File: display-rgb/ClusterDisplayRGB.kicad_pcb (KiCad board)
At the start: 4 copper layers, 211 x 101.8 mm, 137 parts, among them J1 Verdin iMX95 Hexa 8GB WB IT, J10 RTC coin cell, J11 Molex KK-254 22-27-2041, rota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, J12 Samtec TSW-103-07-G-S A55 con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, J13 Samtec TSW-105-07-G-S USB_1 O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, J14 PLACEHOLDER 50-pin FPC for th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, J2 Phoenix MKDS 1,5/3-5,08 power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, J3 Molex KK-254 22-27-2031 priva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, J4 TST040HDBC-42 panel, J8 Samtec TSW-108-07-G-S JTAG (b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, J9 Samtec TSW-104-07-G-S buttons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, Q1 PMV55ENEA (AEC-Q101, 60V/20V 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, Q2 PMV55ENEA (AEC-Q101, 60V/20V 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, Q3 PMV55ENEA ignition wake pulld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, U1 LM74930-Q1, U10 TLV733P-Q1 3.3V (AEC-Q100 G1), U2 LM61460-Q1, U3 TLV767-Q1, U4 TCAN1044V-Q1, U6 TPS65131-Q1, U7 TPS61165-Q1, U8 TPS22918-Q1 (AEC-Q100 G2) dia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, U9 DS90CF384AQ-Q1

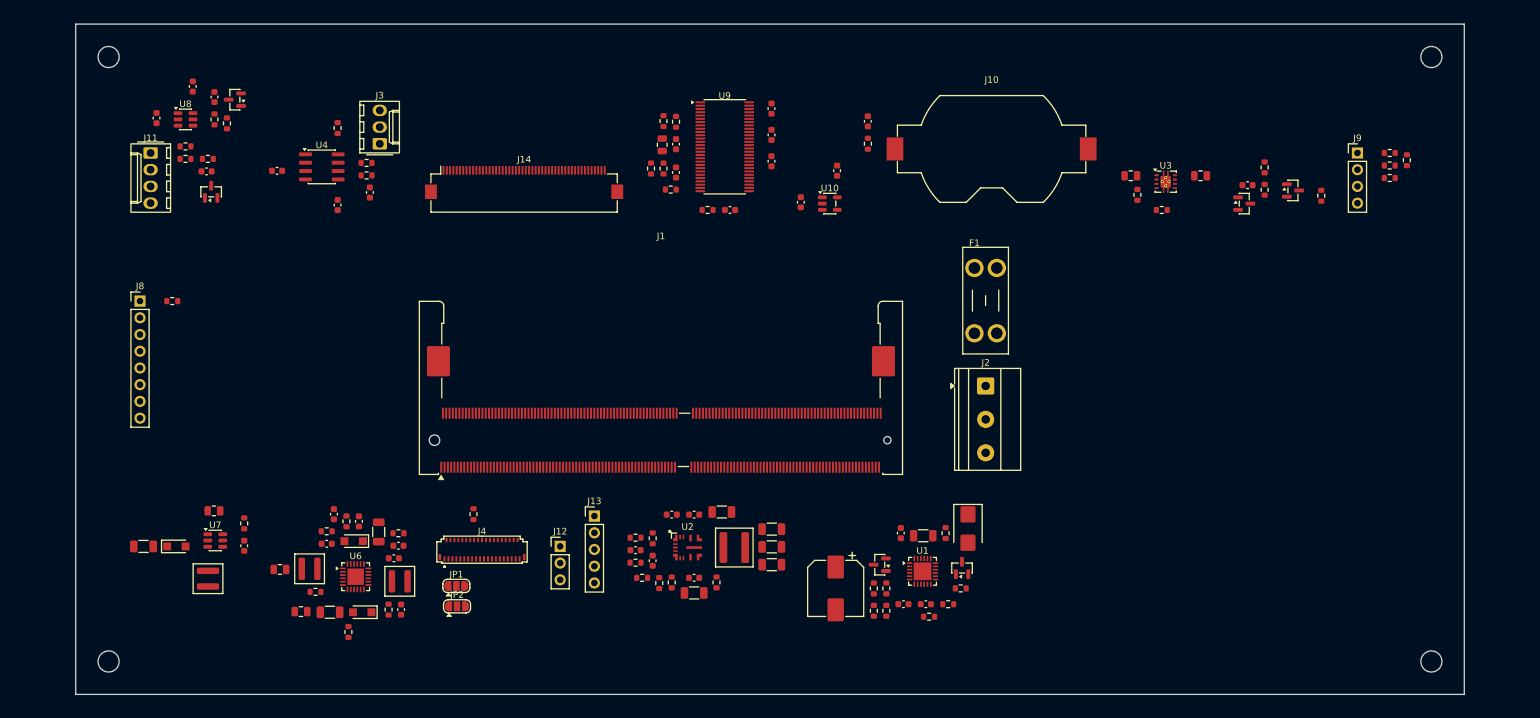
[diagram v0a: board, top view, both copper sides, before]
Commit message: Six layers with solid GND planes, a field-solved DSI geometry, and the RGB variant routed
Both boards and display-rgb/ move to JLC06161H-3313 six-layer: F / In1 GND /
In2 / In3 with the +5V or +3V3 pour / In4 GND / B. Every net class except GND
is restricted to F, In2, In3 and B in the router input (FreeRouting 2.2.4
ignores a layer_rule "active off"), and review/layout_checks.py now fails a
board with any track on In1 or In4. All three boards: 0 unconnected under
kicad-cli DRC, accepted categories only, no copper but GND fill on the planes.

- DSI pairs are 0.16 mm, field-solved on the new stack-up at 96.4-103.1 ohm
  differential (review/dsi_impedance.py); board minimum track 0.15 mm.
- gauges/ routes VIN_PROT, VIN_FUSED and +5V at 0.4 mm from the start; every
  power net now passes the 20 K current check, and nothing crosses the buck's
  switch node (P-07).
- Panel bias +5.98 V / -6.05 V, inside the ICNL9707's rating; fab/README.md
  gives a diode-test check of the panel's pin polarity before JP1/JP2.
- display-rgb/ brought up to date with display/ (standoffs, FETs, audio,
  USB-C, MFi header), RGB parts renumbered, routed; still not a fab candidate
  while its panel connector is a placeholder.
- FreeRouting runs end at routing: (postroute off) in the DSN, a job timeout
  as backstop; one in-place attempt, since retries of one DSN are identical.
- The OV/UV divider tops are pulled to the LM74930 SW pin.
- docs/electrical-review.md section 8b records the measured results; the
  display/ battery path on inner copper (D-02 residual) is still open.

Co-Authored-By: Claude Opus 5.5 <noreply@anthropic.com>
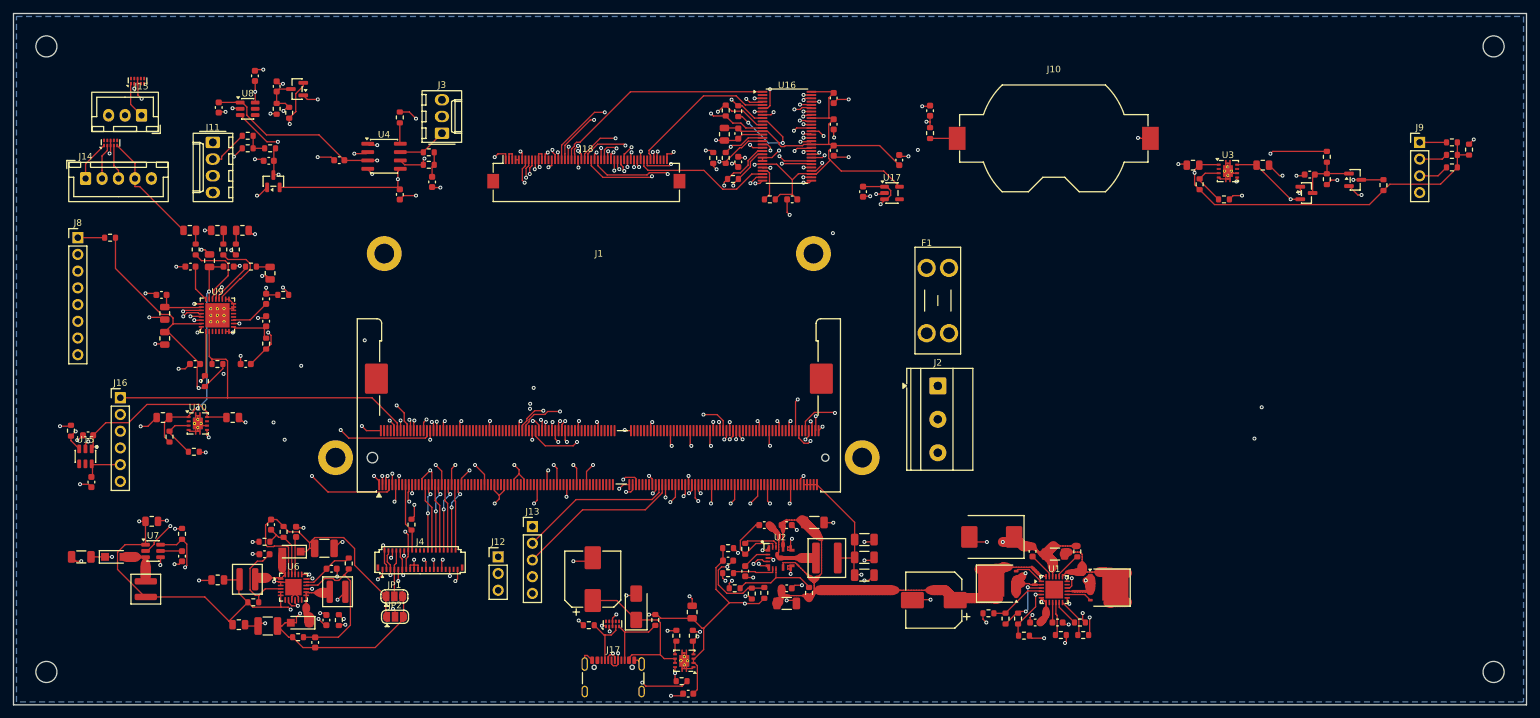
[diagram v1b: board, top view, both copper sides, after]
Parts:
- added C73: 1u MICBIAS, Capacitor_SMD:C_0603_1608Metric, F.Cu at (133.5, 142.7)
- added C74: 1u mic AC couple, Capacitor_SMD:C_0603_1608Metric, F.Cu at (130.4, 149.2)
- added C75: 1u mic AC couple, Capacitor_SMD:C_0603_1608Metric, F.Cu at (133.5, 139.3)
- added C76: 4.7u line-out DC block, Capacitor_SMD:C_0805_2012Metric, F.Cu at (134.1, 135.4)
- added C77: 4.7u line-out DC block, Capacitor_SMD:C_0805_2012Metric, F.Cu at (126.1, 128.9)
- added C78: 4.7u line-out DC block, Capacitor_SMD:C_0805_2012Metric, F.Cu at (129.9, 128.9)
- added C79: 4.7u line-out DC block, Capacitor_SMD:C_0805_2012Metric, F.Cu at (121.9, 128.9)
- added C80: 100n USB switch IN, Capacitor_SMD:C_0603_1608Metric, F.Cu at (197.6, 199.3)
- added C81: 10u USB switch IN, Capacitor_SMD:C_0805_2012Metric, F.Cu at (198.2, 186.9)
- added C82: 100u 35V hybrid polymer VBUS (Panasonic EEH-ZA1V101P), Capacitor_SMD:CP_Elec_8x10, F.Cu at (183.1, 181.9)
- added C83: 1u MFi switch CIN, Capacitor_SMD:C_0603_1608Metric, F.Cu at (106.4, 160.1)
- added C84: 1u MFi 5V out, Capacitor_SMD:C_0603_1608Metric, F.Cu at (106.9, 167.2)
- added C85: 1u LDO input (AEC-Q200), Capacitor_SMD:C_0603_1608Metric, F.Cu at (224.1, 123.0)
- added C86: 1u LDO output (AEC-Q200), Capacitor_SMD:C_0603_1608Metric, F.Cu at (229.6, 118.2)
- added C87: 100n receiver VCC decoupling (AEC-Q200), Capacitor_SMD:C_0603_1608Metric, F.Cu at (213.4, 124.2)
- added C88: 100n receiver VCC decoupling (AEC-Q200), Capacitor_SMD:C_0603_1608Metric, F.Cu at (219.7, 116.8)
- added C89: 100n receiver VCC decoupling (AEC-Q200), Capacitor_SMD:C_0603_1608Metric, F.Cu at (219.7, 112.8)
- added C90: 100n receiver VCC decoupling (AEC-Q200), Capacitor_SMD:C_0603_1608Metric, F.Cu at (219.7, 108.8)
- added C91: 100n receiver VCC decoupling (AEC-Q200), Capacitor_SMD:C_0603_1608Metric, F.Cu at (205.2, 114.2)
- added C92: 100n receiver VCC decoupling (AEC-Q200), Capacitor_SMD:C_0603_1608Metric, F.Cu at (205.2, 118.5)
- added C93: 10u receiver bulk (AEC-Q200), Capacitor_SMD:C_0805_2012Metric, F.Cu at (203.1, 114.3)
- added D8: SMAJ5.0A VBUS TVS, Diode_SMD:D_SMA, F.Cu at (189.7, 186.1)
- added J15: JST XH B3B-XH-A electret microphone (2-wire + shield), Connector_JST:JST_XH_B3B-XH-A_1x03_P2.50mm_Vertical, F.Cu at (114.5, 111.5)
- added J16: MFi daughterboard header I2C_1, reset, switched 5V, 1V8 (DN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, Connector_PinHeader_2.54mm:PinHeader_1x06_P2.54mm_Vertical, F.Cu at (111.3, 154.4)
- added J17: GCT USB4105-GF-A USB-C 2.0 host receptacle, Connector_USB:USB_C_Receptacle_GCT_USB4105-xx-A_16P_TopMnt_Horizontal, F.Cu at (186.2, 197.9)
- added J18: PLACEHOLDER 50-pin FPC for the RGB panel (pinout TBD), Connector_FFC-FPC:Hirose_FH12-50S-0.5SH_1x50-1MP_P0.50mm_Horizontal, F.Cu at (182.1, 120.0)
- added R65: 100R line-out series, Resistor_SMD:R_0603_1608Metric, F.Cu at (131.2, 134.4)
- added R66: 100R line-out series, Resistor_SMD:R_0603_1608Metric, F.Cu at (127.0, 131.8)
- added R67: 100R line-out series, Resistor_SMD:R_0603_1608Metric, F.Cu at (128.9, 131.8)
- added R68: 100R line-out series, Resistor_SMD:R_0603_1608Metric, F.Cu at (122.8, 131.8)
- added R69: 61.9k 1% USB ILIM (1.6-2.0 A), Resistor_SMD:R_0603_1608Metric, F.Cu at (195.8, 190.5)
- added R70: 100k FAULT pull-up to +1V8, Resistor_SMD:R_0603_1608Metric, F.Cu at (196.6, 197.4)
- added R71: 22k Rp CC1 (1.5 A, +/-5 percent or better), Resistor_SMD:R_0603_1608Metric, F.Cu at (182.5, 188.9)
- added R72: 22k Rp CC2 (1.5 A, +/-5 percent or better), Resistor_SMD:R_0603_1608Metric, F.Cu at (192.6, 188.1)
- added R73: 100k USB EN pull-down, Resistor_SMD:R_0603_1608Metric, F.Cu at (198.3, 190.5)
- added R74: 100k MFi switch off in reset, Resistor_SMD:R_0603_1608Metric, F.Cu at (103.8, 159.4)
- added R75: 100R LVDS pair termination, Resistor_SMD:R_0603_1608Metric, F.Cu at (205.2, 110.8)
- added R76: 100R LVDS pair termination, Resistor_SMD:R_0603_1608Metric, F.Cu at (203.3, 110.7)
- added R77: 100R LVDS pair termination, Resistor_SMD:R_0603_1608Metric, F.Cu at (203.3, 117.9)
- added R78: 100R LVDS pair termination, Resistor_SMD:R_0603_1608Metric, F.Cu at (204.4, 121.1)
- added R79: 100R LVDS pair termination, Resistor_SMD:R_0603_1608Metric, F.Cu at (201.4, 117.9)
- added R80: 10k PWR_DWN pull-up (always enabled), Resistor_SMD:R_0603_1608Metric, F.Cu at (210.0, 124.2)
- added S1: M2x0.4 SMD standoff 2.5 mm, MountingHole:MountingHole_2.2mm_M2_Pad, F.Cu at (151.4, 132.5)
- added S2: M2x0.4 SMD standoff 2.5 mm, MountingHole:MountingHole_2.2mm_M2_Pad, F.Cu at (216.6, 132.5)
- added S3: M2x0.4 SMD standoff 7.0 mm, MountingHole:MountingHole_2.2mm_M2_Pad, F.Cu at (144.0, 163.5)
- added S4: M2x0.4 SMD standoff 7.0 mm, MountingHole:MountingHole_2.2mm_M2_Pad, F.Cu at (224.0, 163.5)
- added U11: TPS2557-Q1, Package_DFN_QFN:Texas_DRB0008A, F.Cu at (197.0, 194.3)
- added U12: TPD4E02B04-Q1 line-out ESD (bidirectional, review D-11), Package_SON:USON-10_2.5x1.0mm_P0.5mm, F.Cu at (109.8, 115.7)
- added U13: TPD4E05U06-Q1 mic ESD, Package_SON:USON-10_2.5x1.0mm_P0.5mm, F.Cu at (113.9, 106.2)
- added U14: TPD4E05U06-Q1 USB ESD, Package_SON:USON-10_2.5x1.0mm_P0.5mm, F.Cu at (186.1, 188.7)
- added U15: TPS22918-Q1 (AEC-Q100 G2) MFi 5V switch, Package_TO_SOT_SMD:SOT-23-6, F.Cu at (106.0, 163.3)
- added U16: DS90CF384AQ-Q1, Package_SO:TSSOP-56_6.1x14mm_P0.5mm, F.Cu at (212.6, 114.6)
- added U17: TLV733P-Q1 3.3V (AEC-Q100 G1), Package_TO_SOT_SMD:SOT-23-5, F.Cu at (228.5, 123.2)
- C46, C47: footprint Capacitor_SMD:C_1206_3216Metric -> Capacitor_SMD:C_1210_3225Metric
- C64: value 1u LDO input (AEC-Q200) -> 10u CIN; footprint Capacitor_SMD:C_0603_1608Metric -> Capacitor_SMD:C_0805_2012Metric
- C65: value 1u LDO output (AEC-Q200) -> 10u COUT; footprint Capacitor_SMD:C_0603_1608Metric -> Capacitor_SMD:C_0805_2012Metric
- C66: value 100n receiver VCC decoupling (AEC-Q200) -> 10u AVDD; footprint Capacitor_SMD:C_0603_1608Metric -> Capacitor_SMD:C_0805_2012Metric
- C67: value 100n receiver VCC decoupling (AEC-Q200) -> 100n AVDD
- C68: value 100n receiver VCC decoupling (AEC-Q200) -> 10u DREG; footprint Capacitor_SMD:C_0603_1608Metric -> Capacitor_SMD:C_0805_2012Metric
- C69: value 100n receiver VCC decoupling (AEC-Q200) -> 100n DREG
- C70: value 100n receiver VCC decoupling (AEC-Q200) -> 10u IOVDD; footprint Capacitor_SMD:C_0603_1608Metric -> Capacitor_SMD:C_0805_2012Metric
- C71: value 100n receiver VCC decoupling (AEC-Q200) -> 100n IOVDD
- C72: value 10u receiver bulk (AEC-Q200) -> 1u VREF; footprint Capacitor_SMD:C_0805_2012Metric -> Capacitor_SMD:C_0603_1608Metric
- D1: footprint Diode_SMD:D_SMB -> Diode_SMD:D_SMC
- J14: value PLACEHOLDER 50-pin FPC for the RGB panel (pinout TBD) -> JST XH B5B-XH-A balanced line-out L/R; footprint Connector_FFC-FPC:Hirose_FH12-50S-0.5SH_1x50-1MP_P0.50mm_Horizontal -> Connector_JST:JST_XH_B5B-XH-A_1x05_P2.50mm_Vertical
- Q1: value PMV55ENEA (AEC-Q101, 60V/20V VGS) diode -> SQJ460AEP (AEC-Q101, 60V/20V VGS) diode; footprint Package_TO_SOT_SMD:SOT-23 -> Package_SO:PowerPAK_SO-8L_Single
- Q2: value PMV55ENEA (AEC-Q101, 60V/20V VGS) pass -> SQJ460AEP (AEC-Q101, 60V/20V VGS) pass; footprint Package_TO_SOT_SMD:SOT-23 -> Package_SO:PowerPAK_SO-8L_Single
- R38: value 562k VPOS top R1 (see docstring) -> 511k VPOS top R1 (see docstring)
- R40: value 536k VNEG top R3 (see docstring) -> 499k VNEG top R3 (see docstring)
- R59: value 100R LVDS pair termination -> 316k 1% FB top
- R60: value 100R LVDS pair termination -> 100k FB bot
- R61: value 100R LVDS pair termination -> 2.2k I2C1 SDA pull-up
- R62: value 100R LVDS pair termination -> 2.2k I2C1 SCL pull-up
- R63: value 100R LVDS pair termination -> 2.2k mic bias
- R64: value 10k PWR_DWN pull-up (always enabled) -> 100R mic return
- U10: value TLV733P-Q1 3.3V (AEC-Q100 G1) -> TLV767-Q1 (3.3 V audio AVDD); footprint Package_TO_SOT_SMD:SOT-23-5 -> Package_DFN_QFN:Texas_DRB0008A
- U9: value DS90CF384AQ-Q1 -> TAC5112-Q1; footprint Package_SO:TSSOP-56_6.1x14mm_P0.5mm -> Package_DFN_QFN:QFN-32-1EP_5x5mm_P0.5mm_EP3.7x3.7mm_ThermalVias
- moved C65 109.1 mm to (117.8, 157.4), turned to 180 degrees
- moved U10 101.7 mm to (123.1, 158.3)
- moved C69 96.9 mm to (117.6, 138.7), turned to 180 degrees
- moved C68 96.1 mm to (118.1, 141.5)
- moved C64 92.3 mm to (128.4, 157.4), turned to 0 degrees
- moved R59 90.6 mm to (118.8, 160.3)
- moved R60 87.3 mm to (122.5, 162.6), turned to 0 degrees
- moved C67 84.0 mm to (127.8, 134.4), turned to 0 degrees
- moved C70 83.1 mm to (118.1, 145.3)
- moved U9 81.2 mm to (126.1, 141.8)
- moved C66 79.4 mm to (124.9, 133.5), turned to 90 degrees
- moved C71 78.7 mm to (122.7, 149.2), turned to 180 degrees
- moved R62 76.5 mm to (124.2, 151.8), turned to -90 degrees
- moved C72 74.0 mm to (122.0, 134.4), turned to 180 degrees
- moved R61 74.0 mm to (126.1, 149.2), turned to 0 degrees
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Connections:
- C68 pad 1: +3V3 -> CODEC_DREG
- C69 pad 1: +3V3 -> CODEC_DREG
- C70 pad 1: +3V3 -> +1V8
- C71 pad 1: +3V3 -> +1V8
- C72 pad 1: +3V3 -> CODEC_VREF
- J1 pad 12: (no net) -> I2C1_SDA
- J1 pad 14: (no net) -> I2C1_SCL
- J1 pad 181: (no net) -> USB2_DN
- J1 pad 183: (no net) -> USB2_DP
- J1 pad 185: (no net) -> USB2_EN
- J1 pad 187: (no net) -> USB2_OC_N
- J1 pad 208: RGB_RESET -> MFI_RST_N
- J1 pad 210: (no net) -> MFI_PWR_EN
- J1 pad 212: (no net) -> RGB_RESET
- J1 pad 30: (no net) -> I2S_BCLK
- J1 pad 32: (no net) -> I2S_FSYNC
- J1 pad 34: (no net) -> I2S_DIN
- J1 pad 36: (no net) -> I2S_DOUT
- J14 pad 1: GND -> LINE_L_P
- J14 pad 2: RGB_LEDK -> LINE_L_N
- J14 pad 3: RGB_LEDK -> LINE_R_P
- J14 pad 4: RGB_LEDA -> LINE_R_N
- J14 pad 5: RGB_LEDA -> GND
- Q1 pad 1: DGATE -> COMMON
- Q1 pad 3: +12V_PROT -> COMMON
- Q2 pad 1: HGATE -> COMMON
- Q2 pad 3: SENSE_OUT -> COMMON
- R59 pad 1: LVDS_D0_P -> +3V3
- R59 pad 2: LVDS_D0_N -> FB_3V3
- R60 pad 1: LVDS_D1_P -> FB_3V3
- R60 pad 2: LVDS_D1_N -> GND
- R61 pad 1: LVDS_D2_P -> I2C1_SDA
- R61 pad 2: LVDS_D2_N -> +1V8
- R62 pad 1: LVDS_D3_P -> I2C1_SCL
- R62 pad 2: LVDS_D3_N -> +1V8
- R63 pad 1: LVDS_CLK_P -> CODEC_MICBIAS
- R63 pad 2: LVDS_CLK_N -> MIC_P
- R64 pad 1: +3V3 -> MIC_N
- R64 pad 2: RGB_PWRDN -> GND
- U10 pad 1: +5V -> +3V3
- U10 pad 2: GND -> (no net)
- U10 pad 3: +5V -> FB_3V3
- U10 pad 4: (no net) -> GND
- U10 pad 5: +3V3 -> PWR_EN_MOCI
- U9 pad 1: RGB_B5 -> GND
- U9 pad 10: LVDS_D0_P -> I2C1_SDA
- U9 pad 11: LVDS_D1_N -> (no net)
- U9 pad 12: LVDS_D1_P -> (no net)
- U9 pad 13: +3V3 -> (no net)
- U9 pad 14: GND -> (no net)
- U9 pad 15: LVDS_D2_N -> GND
- U9 pad 16: LVDS_D2_P -> GND
- U9 pad 17: LVDS_CLK_N -> CODEC_MICBIAS
- U9 pad 18: LVDS_CLK_P -> MIC_IN_P
- U9 pad 19: LVDS_D3_N -> MIC_IN_N
- U9 pad 2: (no net) -> CODEC_DREG
- U9 pad 20: LVDS_D3_P -> (no net)
- U9 pad 21: GND -> (no net)
- U9 pad 23: +3V3 -> GND
- U9 pad 25: RGB_PWRDN -> GND
- U9 pad 26: RGB_PCLK -> GND
- U9 pad 27: RGB_R0 -> AOUT_L_N
- U9 pad 28: GND -> AOUT_L_P
- U9 pad 29: RGB_R1 -> AOUT_R_P
- U9 pad 3: RGB_HS -> I2S_BCLK
- U9 pad 30: RGB_R2 -> AOUT_R_N
- U9 pad 32: RGB_R3 -> CODEC_VREF
- U9 pad 33: RGB_R4 -> GND
- U9 pad 4: GND -> I2S_FSYNC
- U9 pad 5: RGB_VS -> I2S_DOUT
- U9 pad 6: RGB_DE -> I2S_DIN
- U9 pad 7: RGB_R6 -> +1V8
- U9 pad 9: LVDS_D0_N -> I2C1_SCL
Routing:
- net +5V: track 0.00 -> 527.5 mm, vias 0 -> 12
- net +1V8: track 0.00 -> 452.2 mm, vias 0 -> 7
- net GND: track 0.00 -> 362.2 mm, vias 0 -> 170
- net RESET_MICO: track 0.00 -> 231.2 mm, vias 0 -> 1
- net PWR_EN_MOCI: track 0.00 -> 182.4 mm, vias 0 -> 3
- net RESET_MOCI: track 0.00 -> 135.2 mm, vias 0 -> 3
- net PWR_BTN: track 0.00 -> 130.5 mm, vias 0 -> 2
- net RECOVERY: track 0.00 -> 130.5 mm, vias 0 -> 2
- net DIAL_CLICK: track 0.00 -> 118.3 mm, vias 0 -> 3
- net +3V3_RGB: track 0.00 -> 118.1 mm, vias 0 -> 3
- net SLEEP_MOCI: track 0.00 -> 117.4 mm, vias 0 -> 3
- net IGN_WAKE_N: track 0.00 -> 116.6 mm, vias 0 -> 3
- net MFI_PWR_EN: track 0.00 -> 107.3 mm, vias 0 -> 2
- net MFI_RST_N: track 0.00 -> 94.6 mm, vias 0 -> 1
- net VBAT_F: track 0.00 -> 85.2 mm, vias 0 -> 2
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- added copper zone on In3.Cu, net +5V
- added copper zone on B.Cu, net GND
- added copper zone on In1.Cu, net GND
- added copper zone on In2.Cu, net GND
- added copper zone on In4.Cu, net GND
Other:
- board size 211 x 101.8 mm -> 229.9 x 105 mm
- copper layers 4 -> 6

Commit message: Keep the display battery path on outer copper, pour it, and rate it along the real current path
VBAT_IN, VBAT_F, SENSE_OUT, COMMON and +12V_PROT (2.6 A behind the 5 A
fuse) now have their own router net class on F.Cu/B.Cu only, at 0.3 mm
with a 1.0/0.5 mm via, and an F.Cu pour in a 2 mm band around their own
tracks after widening. No battery copper is left on the 0.5 oz inner
layers (about 60 mm of VBAT_F was), on display/ and display-rgb/.

layout_checks.py rates these nets along the path the current takes,
including same-net fill and via barrels, and lists milliamp branches
apart. VBAT_IN and VBAT_F pass on both boards; the remaining necks
(+12V_PROT, COMMON, SENSE_OUT, at most 20 mW each at 2.6 A) are
documented in docs/electrical-review.md section 8b.

route_board.py also gets a hard FreeRouting timeout: a router whose
thread has died never exits. A two-pass route (main path wide, branches
second) was tried and dropped, since FreeRouting 2.2.4 cannot continue
from a board that already has wiring.

Co-Authored-By: Claude Opus 5.5 <noreply@anthropic.com>
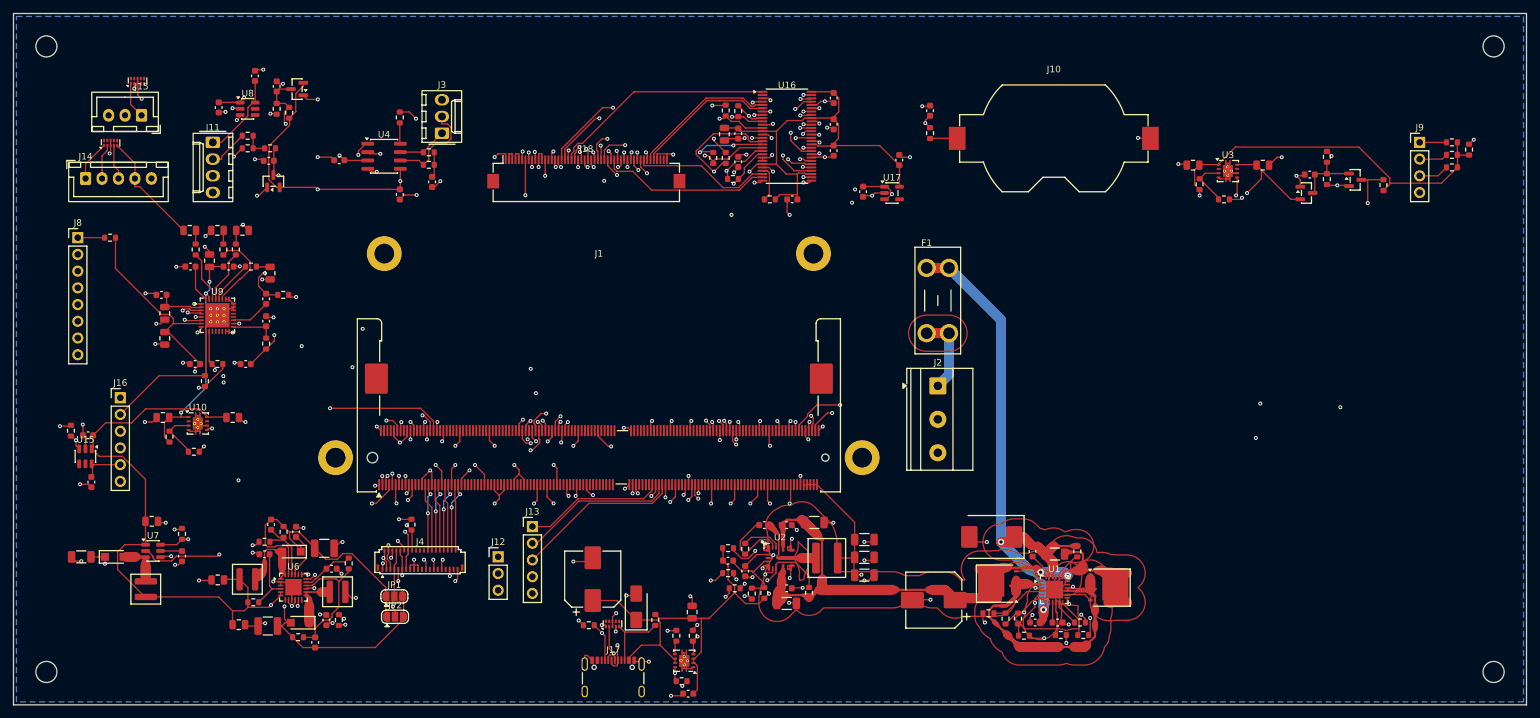
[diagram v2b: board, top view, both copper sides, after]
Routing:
- net +5V: track 527.5 -> 549.1 mm, vias 12 -> 10
- net COMMON: track 24.9 -> 44.2 mm, vias 2 -> 0
- net LVDS_D0_N: track 85.2 -> 70.9 mm
- net LVDS_D0_P: track 80.4 -> 66.3 mm, vias 3 -> 2
- net RGB_SPI_SDA: track 66.5 -> 77.3 mm
- net SLEEP_MOCI: track 117.4 -> 128.1 mm
- net LVDS_D1_P: track 75.6 -> 66.2 mm
- net I2C1_SCL: track 57.6 -> 66.9 mm, vias 2 -> 1
- net PWR_EN_MOCI: track 182.4 -> 191.4 mm, vias 3 -> 4
- net +3V3_RGB: track 118.1 -> 109.2 mm
- net LVDS_D2_N: track 61.1 -> 69.2 mm, vias 2 -> 3
- net FB_5V: track 19.7 -> 11.8 mm, vias 2 -> 0
- net RGB_R1: track 32.5 -> 39.1 mm, vias 2 -> 3
- net JTAG_VREF: track 76.3 -> 82.8 mm
- net +1V8: track 452.2 -> 446.4 mm, vias 7 -> 9
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- added copper zone on F.Cu, net +12V_PROT
- added copper zone on F.Cu, net COMMON
- added copper zone on F.Cu, net SENSE_OUT
- added copper zone on F.Cu, net VBAT_F
- added copper zone on F.Cu, net VBAT_IN
